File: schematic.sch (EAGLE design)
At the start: 15 parts, among them J1 FTDI_DEVICERA_SMT, M1 WIRELESS-NRF24L01, U1 ATMEGA328P_TQFP, U2 GY-521MPU6050

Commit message: Added (mostly compelte) v-reg circuit
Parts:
- added BATTERY_JST: Battery_JST, quad:JST_CONNECTOR_FEMALE
- added C10: 22uF, SparkFun-Passives:CAP0603-CAP
- added C11, C5: 10uF, SparkFun-Passives:CAP0603-CAP
- added C6: 10pF, SparkFun-Passives:CAP0603-CAP
- added C7, C9: (no value), SparkFun-Passives:CAP0603-CAP
- added C8: 0.1uF, SparkFun-Passives:CAP0603-CAP
- added L1: 1uH, rcl:L-USL1812
- added R6: 1.12M, resistor:R-US_M2309
- added R7: 200K, resistor:R-US_M2309
- added R8: 1M, resistor:R-US_M2309
- added U3: TPS63060, SparkFun-PowerIC:TPS63060
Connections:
- new net N$27: L1.1, U3.L1
- new net N$28: L1.2, U3.L2
- new net N$29: R4.2
- new net N$31: C10.2, C7.2, C9.2, R6.2, R8.2, U3.VOUT
- new net N$32: C6.2, R6.1, R7.2, U3.FB
- new net N$33: C8.2, U3.VAUX
- new net N$34: R8.1, U3.PG
- net GND: now also BATTERY_JST.-, C10.1, C5.1, C6.1, C7.1, C8.1, C9.1, R7.1, U3.GND, U3.PGND@1, U3.PGND@2, U3.PGND@3, U3.PGND@4, U3.PGND@5, U3.PGND@6, U3.PGND@7, U3.PGND@8, U3.PGND@PAD, U3.PS/SYNC
- net VCC: now also BATTERY_JST.+, C11.2, C5.2, U3.EN, U3.VIN; no longer R4.2

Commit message: completed v_reg external, decouplng, labels
Need work on adding control switches, indicator LEDs. Need to find all correct parts and replace current placeholder symbols
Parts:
- removed BATTERY_JST: Battery_JST, quad:JST_CONNECTOR_FEMALE
- removed R4, R5: 10K, SparkFun-Passives:RESISTOR0603-RES
- added C12: 100uF, SparkFun-Passives:CAP0603-CAP
- added C13: 10uF, SparkFun-Passives:CAP0603-CAP
- added C14: 100nF, SparkFun-Passives:CAP0603-CAP
- added C15: 0.1uF, SparkFun-Passives:CAP0603-CAP
- added R10, R9: 10M, resistor:R-US_M2309
- added U$1: JST_CONNECTOR_FEMALE, quad:JST_CONNECTOR_FEMALE
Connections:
- net N$10 renamed SDA
- net N$11 renamed SCL
- net N$14 renamed MISO
- net N$15 renamed MOSI
- net N$16 renamed SCK
- net N$19 renamed CE
- net N$20 renamed CSN
- net N$3 renamed TXD
- net N$5 renamed DTR
- net N$7 renamed RXD
- removed net N$12: U1.PD3(INT1)
- removed net N$13: U1.PB1(OC1A)
- removed net N$17: R1.2
- removed net N$18: C3.1, J1.VCC, U1.VCC@4, U1.VCC@6
- removed net N$21: R2.2
- removed net N$22: R3.2
- removed net N$23: U2.VCC
- removed net N$24: M1.VCC
- removed net N$26: C4.1, U1.AVCC
- removed net N$29: R4.2
- removed net N$31: C10.2, C7.2, C9.2, R6.2, R8.2, U3.VOUT
- removed net N$6: R4.1, R5.2, U1.PC2(ADC2)
- removed net N$8: U1.PD5(T1)
- removed net N$9: U1.PD6(AIN0)
- new net V_BAT: R10.2, R9.1, U1.PC2(ADC2)
- new net V_REG_OUT: C10.2, C13.2, C14.2, C15.2, C3.1, C4.1, C7.2, C9.2, J1.VCC, M1.VCC, R1.2, R2.2, R3.2, R6.2, R8.2, U1.AVCC, U1.VCC@4, U1.VCC@6, U2.VCC, U3.VOUT
- net GND: now also C12.1, C13.1, C14.1, C15.1, R10.1, U$1.-; no longer BATTERY_JST.-, R5.1
- net VCC: now also C12.2, R9.2, U$1.+; no longer BATTERY_JST.+
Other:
- note added: "BATTERY"
- moved on the sheet: J1, M1, R2, R3

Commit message: Added LEDs, switches, motor circuit, and made it look pretty
Still need to get all the correct parts to replace place-holder
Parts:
- added LED1: RED, led:LED
- added LED2: (no value), led:LED
- added S2: PUSH_BUTT, quad:SWITCH-MOMENTARY-2SMD
- added S3: (no value), SparkFun:SWITCH-SPST-SMD-A
- added U$10, U$13, U$4, U$7: JST_CONNECTOR_FEMALE, quad:JST_CONNECTOR_FEMALE
- added U$11, U$2, U$5, U$8: N-CHANNEL-MOSFET-IRLML6244TRPBF, quad:N-CHANNEL-MOSFET-IRLML6244TRPBF
- added U$12, U$3, U$6, U$9: DB2W40300L, quad:DB2W40300L
- R2, R3: value 10K -> 100; device SparkFun-Resistors:10KOHM-1/10W-1%(0603)0603 -> resistor:R-US_M2309
- S1: device SparkFun:TAC_SWITCHSMD -> SparkFun:SWITCH-SPST-SMD-A
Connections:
- net N$34 renamed PG
- new net N$10: LED1.A, R2.1
- new net N$11: LED2.A, R3.1
- new net N$3: U$2.D, U$3.PPIN, U$4.-
- new net N$5: U$5.D, U$6.PPIN, U$7.-
- new net N$6: U$10.-, U$8.D, U$9.PPIN
- new net N$7: U$11.D, U$12.PPIN, U$13.-
- new net N$8: S1.P, S3.P, U$1.+
- new net N$9: S1.S, S3.S
- new net PWM1: U$2.G, U1.PD3(INT1)
- new net PWM2: U$5.G, U1.PD5(T1)
- new net PWM3: U$8.G, U1.PD6(AIN0)
- new net PWM4: U$11.G, U1.PB1(OC1A)
- net GND: now also C11.1, LED1.C, LED2.C, S2.1, U$11.S, U$2.S, U$5.S, U$8.S; no longer S1.1
- net N$2: now also S2.2; no longer S1.3
- net SCL: no longer R3.1
- net SDA: no longer R2.1
- net VCC: now also R2.2, S1.O, S3.O, U$10.+, U$12.GPIN, U$13.+, U$3.GPIN, U$4.+, U$6.GPIN, U$7.+, U$9.GPIN; no longer U$1.+
- net V_REG_OUT: no longer R2.2
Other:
- note added: "2017 - 2018"
- note added: "ADVANCED PROJECTS"
- note added: "BATTERY MANAGEMENT"
- note added: "IEEE@UCLA"
- note added: "MCU PERIPHERALS"
- note added: "MICROCONTROLLER"
- note added: "MOTOR DRIVERS"
- note added: "QUADCOPTER DESIGN"
- note added: "TEAM 5"
- note added: "VOLTAGE REGULATION"
- note removed: "BATTERY"
- moved on the sheet: C1, C10, C11, C12, C13, C14, C15, C2, C3, C4, C5, C6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

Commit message: added pull-down for motor
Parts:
- added R11, R12, R4, R5: 10K, resistor:R-US_M2309
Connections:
- net GND: now also R11.2, R12.2, R4.2, R5.2
- net PWM1: now also R4.1
- net PWM3: now also R11.1
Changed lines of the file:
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@@
 <part name="GND25" library="SparkFun" deviceset="GND" device=""/>
 <part name="R3" library="resistor" library_urn="urn:adsk.eagle:library:348" deviceset="R-US_" device="M2309" package3d_urn="urn:adsk.eagle:package:26085/1" value="100"/>
+<part name="R4" library="resistor" library_urn="urn:adsk.eagle:library:348" deviceset="R-US_" device="M2309" package3d_urn="urn:adsk.eagle:package:26085/1" value="10K"/>
+<part name="GND26" library="SparkFun" deviceset="GND" device=""/>
+<part name="R5" library="resistor" library_urn="urn:adsk.eagle:library:348" deviceset="R-US_" device="M2309" package3d_urn="urn:adsk.eagle:package:26085/1" value="10K"/>
+<part name="GND27" library="SparkFun" deviceset="GND" device=""/>
+<part name="R11" library="resistor" library_urn="urn:adsk.eagle:library:348" deviceset="R-US_" device="M2309" package3d_urn="urn:adsk.eagle:package:26085/1" value="10K"/>
+<part name="GND28" library="SparkFun" deviceset="GND" device=""/>
+<part name="R12" library="resistor" library_urn="urn:adsk.eagle:library:348" deviceset="R-US_" device="M2309" package3d_urn="urn:adsk.eagle:package:26085/1" value="10K"/>
+<part name="GND29" library="SparkFun" deviceset="GND" device=""/>
 </parts>
 <sheets>
@@
 <instance part="GND25" gate="1" x="78.74" y="93.98"/>
 <instance part="R3" gate="G$1" x="78.74" y="116.84" rot="R90"/>
+<instance part="R4" gate="G$1" x="-198.12" y="-2.54" rot="R270"/>
+<instance part="GND26" gate="1" x="-198.12" y="-10.16"/>
+<instance part="R5" gate="G$1" x="-149.86" y="-2.54" rot="R270"/>
+<instance part="GND27" gate="1" x="-149.86" y="-10.16"/>
+<instance part="R11" gate="G$1" x="-198.12" y="-66.04" rot="R270"/>
+<instance part="GND28" gate="1" x="-198.12" y="-73.66"/>
+<instance part="R12" gate="G$1" x="-149.86" y="-66.04" rot="R270"/>
+<instance part="GND29" gate="1" x="-149.86" y="-73.66"/>
 </instances>
 <busses>
@@
 <wire x1="78.74" y1="101.6" x2="78.74" y2="96.52" width="0.1524" layer="91"/>
 </segment>
+<segment>
+<pinref part="R4" gate="G$1" pin="2"/>
+<pinref part="GND26" gate="1" pin="GND"/>
+</segment>
+<segment>
+<pinref part="R5" gate="G$1" pin="2"/>
+<pinref part="GND27" gate="1" pin="GND"/>
+</segment>
+<segment>
+<pinref part="R11" gate="G$1" pin="2"/>
+<pinref part="GND28" gate="1" pin="GND"/>
+</segment>
+<segment>
+<pinref part="R12" gate="G$1" pin="2"/>
+<pinref part="GND29" gate="1" pin="GND"/>
+</segment>
 </net>
 <net name="N$1" class="0">
@@
 <wire x1="-195.58" y1="2.54" x2="-198.12" y2="2.54" width="0.1524" layer="91"/>
 <label x="-198.12" y="2.54" size="1.27" layer="95" rot="R180" xref="yes"/>
+<pinref part="R4" gate="G$1" pin="1"/>
 </segment>
 <segment>
@@
 <wire x1="-195.58" y1="-60.96" x2="-198.12" y2="-60.96" width="0.1524" layer="91"/>
 <label x="-198.12" y="-60.96" size="1.27" layer="95" rot="R180" xref="yes"/>
-</segment>
-<segment>
+<pinref part="R11" gate="G$1" pin="1"/>
+</segment>
+<segment>

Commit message: Fixed all warnings, added more debug LEDs
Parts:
- removed S3: (no value), SparkFun:SWITCH-SPST-SMD-A
- added LED3, LED4: RED, led:LED
- added R13, R14: 100, resistor:R-US_M2309
- C7, C9: value (none) -> 22uF
- LED2: value (none) -> RED
- R10: value 10M -> 5M
- R9: value 10M -> 15M
- S1: value (none) -> MAIN_SWITCH
- Y1: value (none) -> 8Mhz
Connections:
- removed net N$9: S1.S, S3.S
- new net DEBUG_LED1: R13.2, U1.PD2(INT0)
- new net DEBUG_LED2: R14.2, U1.PD4(XCK/T0)
- new net N$12: LED3.A, R13.1
- new net N$13: LED4.A, R14.1
- net GND: now also LED3.C, LED4.C
- net N$8: no longer S3.P
- net PWM2: now also R5.1
- net PWM4: now also R12.1
- net VCC: no longer S3.O
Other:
- moved on the sheet: C13, C14, C3, C4, M1

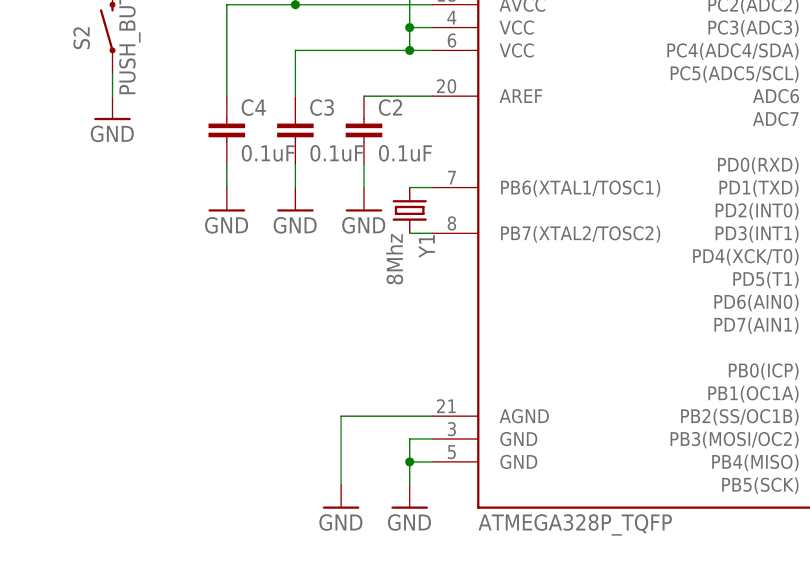
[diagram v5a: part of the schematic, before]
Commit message: Added load capacitor for crystal
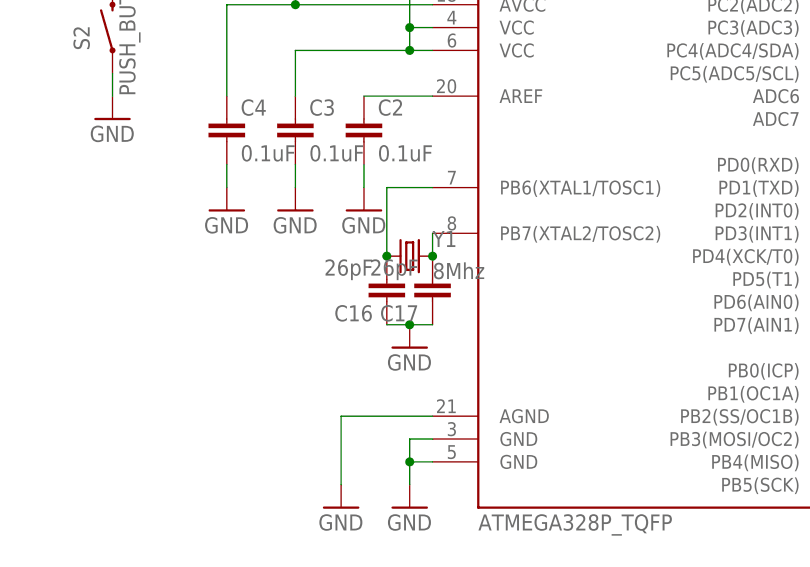
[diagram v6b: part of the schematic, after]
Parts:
- added C16, C17: 26pF, SparkFun-Capacitors:0.1UF-25V-5%(0603)
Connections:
- net GND: now also C16.1, C17.1
- net N$1: now also C16.2
- net N$4: now also C17.2
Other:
- moved on the sheet: Y1
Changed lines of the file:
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@@
 <part name="GND31" library="SparkFun" deviceset="GND" device=""/>
 <part name="R14" library="resistor" library_urn="urn:adsk.eagle:library:348" deviceset="R-US_" device="M2309" package3d_urn="urn:adsk.eagle:package:26085/1" value="100"/>
+<part name="C16" library="SparkFun-Capacitors" deviceset="0.1UF-25V-5%(0603)" device="" value="26pF"/>
+<part name="C17" library="SparkFun-Capacitors" deviceset="0.1UF-25V-5%(0603)" device="" value="26pF"/>
+<part name="GND32" library="SparkFun" deviceset="GND" device=""/>
 </parts>
 <sheets>
@@
 <instance part="GND1" gate="1" x="139.7" y="88.9"/>
 <instance part="GND2" gate="1" x="172.72" y="45.72"/>
-<instance part="Y1" gate="G$1" x="172.72" y="78.74" rot="R270"/>
+<instance part="Y1" gate="G$1" x="172.72" y="73.66"/>
 <instance part="U2" gate="G$1" x="50.8" y="10.16"/>
 <instance part="M1" gate="G$1" x="43.18" y="-45.72"/>
@@
 <instance part="GND31" gate="1" x="-38.1" y="-55.88"/>
 <instance part="R14" gate="G$1" x="-38.1" y="-33.02" rot="R90"/>
+<instance part="C16" gate="G$1" x="170.18" y="71.12" rot="R180"/>
+<instance part="C17" gate="G$1" x="175.26" y="71.12" rot="R180"/>
+<instance part="GND32" gate="1" x="172.72" y="63.5"/>
 </instances>
 <busses>
@@
 <wire x1="-38.1" y1="-48.26" x2="-38.1" y2="-53.34" width="0.1524" layer="91"/>
 </segment>
-</net>
-<net name="N$1" class="0">
-<segment>
-<pinref part="U1" gate="U$1" pin="PB6(XTAL1/TOSC1)"/>
-<pinref part="Y1" gate="G$1" pin="1"/>
-<wire x1="175.26" y1="81.28" x2="172.72" y2="81.28" width="0.1524" layer="91"/>
+<segment>
+<pinref part="C16" gate="G$1" pin="1"/>
+<pinref part="GND32" gate="1" pin="GND"/>
+<wire x1="170.18" y1="66.04" x2="172.72" y2="66.04" width="0.1524" layer="91"/>
+<pinref part="C17" gate="G$1" pin="1"/>
+<wire x1="175.26" y1="66.04" x2="172.72" y2="66.04" width="0.1524" layer="91"/>
+<junction x="172.72" y="66.04"/>
 </segment>
 </net>
@@
 <pinref part="Y1" gate="G$1" pin="2"/>
 <pinref part="U1" gate="U$1" pin="PB7(XTAL2/TOSC2)"/>
-<wire x1="172.72" y1="76.2" x2="175.26" y2="76.2" width="0.1524" layer="91"/>
+<wire x1="175.26" y1="73.66" x2="175.26" y2="76.2" width="0.1524" layer="91"/>
+<pinref part="C17" gate="G$1" pin="2"/>
+<junction x="175.26" y="73.66"/>
 </segment>
 </net>
@@
 </segment>
 </net>
+<net name="N$1" class="0">
+<segment>
+<pinref part="U1" gate="U$1" pin="PB6(XTAL1/TOSC1)"/>
+<pinref part="Y1" gate="G$1" pin="1"/>
+<wire x1="175.26" y1="81.28" x2="170.18" y2="81.28" width="0.1524" layer="91"/>
+<wire x1="170.18" y1="81.28" x2="170.18" y2="73.66" width="0.1524" layer="91"/>
+<pinref part="C16" gate="G$1" pin="2"/>
+<junction x="170.18" y="73.66"/>
+</segment>
+</net>
